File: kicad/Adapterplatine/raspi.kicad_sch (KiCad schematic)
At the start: 8 parts, among them X30 Conn_01x05_Pin, X31 Conn_01x05_Pin, X43 Conn_01x05_Pin

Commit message: Umsortierung/ Erste Leitungung Adapterplatine
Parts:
- added J1: Conn_01x05, Connector_PinSocket_2.54mm:PinSocket_1x05_P2.54mm_Vertical, symbol Connector_Generic:Conn_01x05
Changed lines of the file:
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@@
+	)
+	(symbol
+		(lib_id "Connector_Generic:Conn_01x05")
+		(at 180.34 133.35 270)
+		(unit 1)
+		(body_style 1)
+		(exclude_from_sim no)
+		(in_bom yes)
+		(on_board yes)
+		(in_pos_files yes)
+		(dnp no)
+		(fields_autoplaced yes)
+		(property "Reference" "J1"
+			(at 180.34 137.16 90)
+			(show_name no)
+			(do_not_autoplace no)
+			(effects
+				(font
+					(size 1.27 1.27)
+				)
+			)
+		)
+		(property "Value" "Conn_01x05"
+			(at 180.34 139.7 90)
+			(show_name no)
+			(do_not_autoplace no)
+			(effects
+				(font
+					(size 1.27 1.27)
+				)
+			)
+		)
+		(property "Footprint" "Connector_PinSocket_2.54mm:PinSocket_1x05_P2.54mm_Vertical"
+			(at 180.34 133.35 0)
+			(hide yes)
+			(show_name no)
+			(do_not_autoplace no)
+			(effects
+				(font
+					(size 1.27 1.27)
+				)
+			)
+		)
+		(property "Datasheet" ""
+			(at 180.34 133.35 0)
+			(hide yes)
+			(show_name no)
+			(do_not_autoplace no)
+			(effects
+				(font
+					(size 1.27 1.27)
+				)
+			)
+		)
+		(property "Description" "Generic connector, single row, 01x05, script generated (kicad-library-utils/schlib/autogen/connector/)"
+			(at 180.34 133.35 0)
+			(hide yes)
+			(show_name no)
+			(do_not_autoplace no)
+			(effects
+				(font
+					(size 1.27 1.27)
+				)
+			)
+		)
+		(pin "1"
+		)
+		(pin "3"
+		)
+		(pin "4"
+		)
+		(pin "5"
+		)
+		(pin "2"
+		)
+		(instances
+			(project "Adapterplatine"
+				(path "/99d5d967-6a35-454f-aac3-01cafa1d30b4/6e4113d7-0438-4c79-b883-7b55fbeab670"
+					(reference "J1")
+					(unit 1)
+				)
+			)
+		)
 	)
 	(symbol

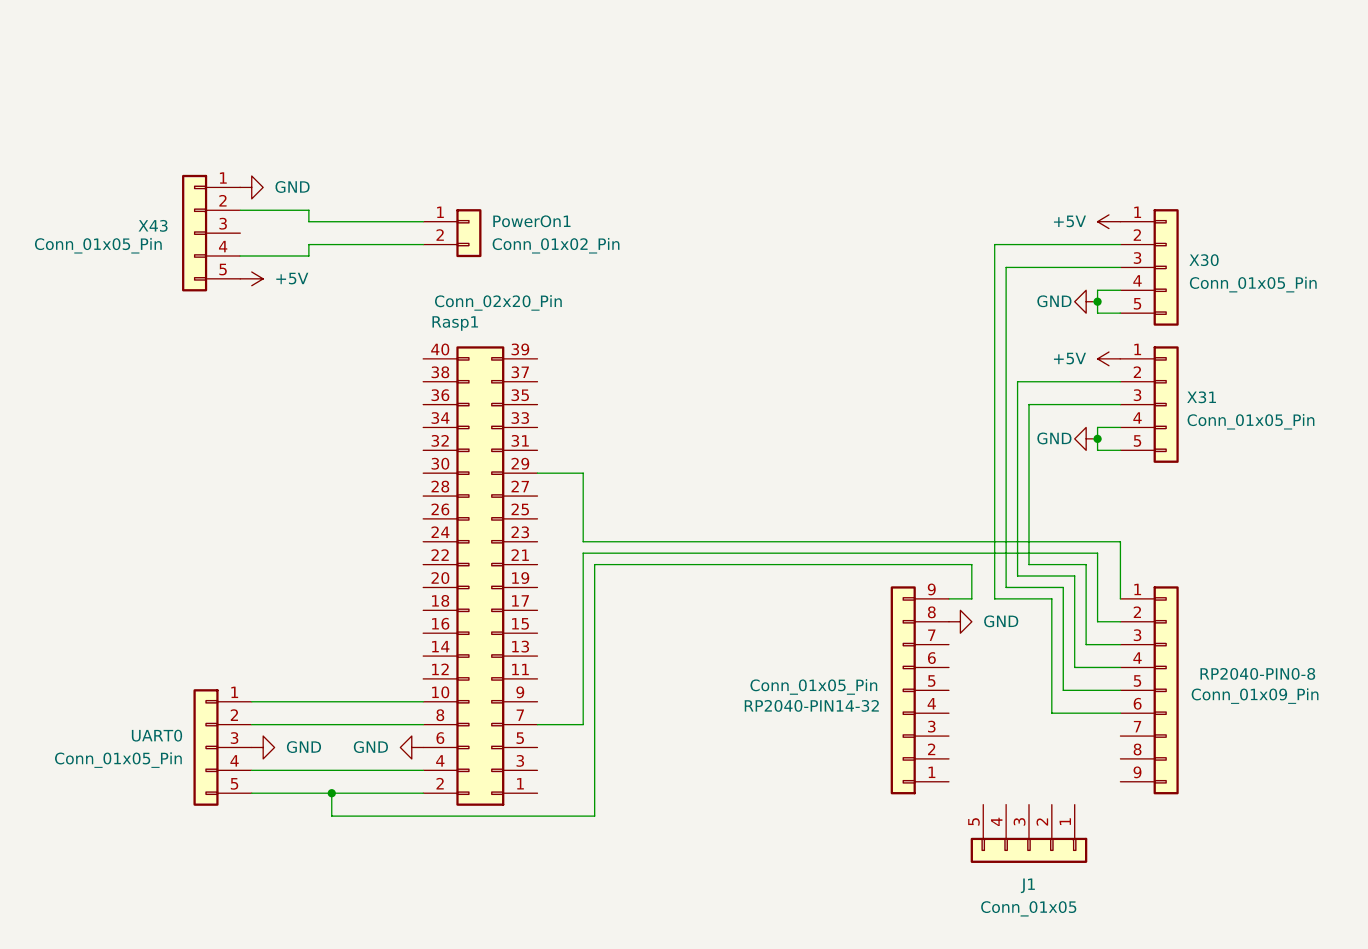
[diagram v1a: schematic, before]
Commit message: Leitungsverlegung Adapterplatine abgeschlossen
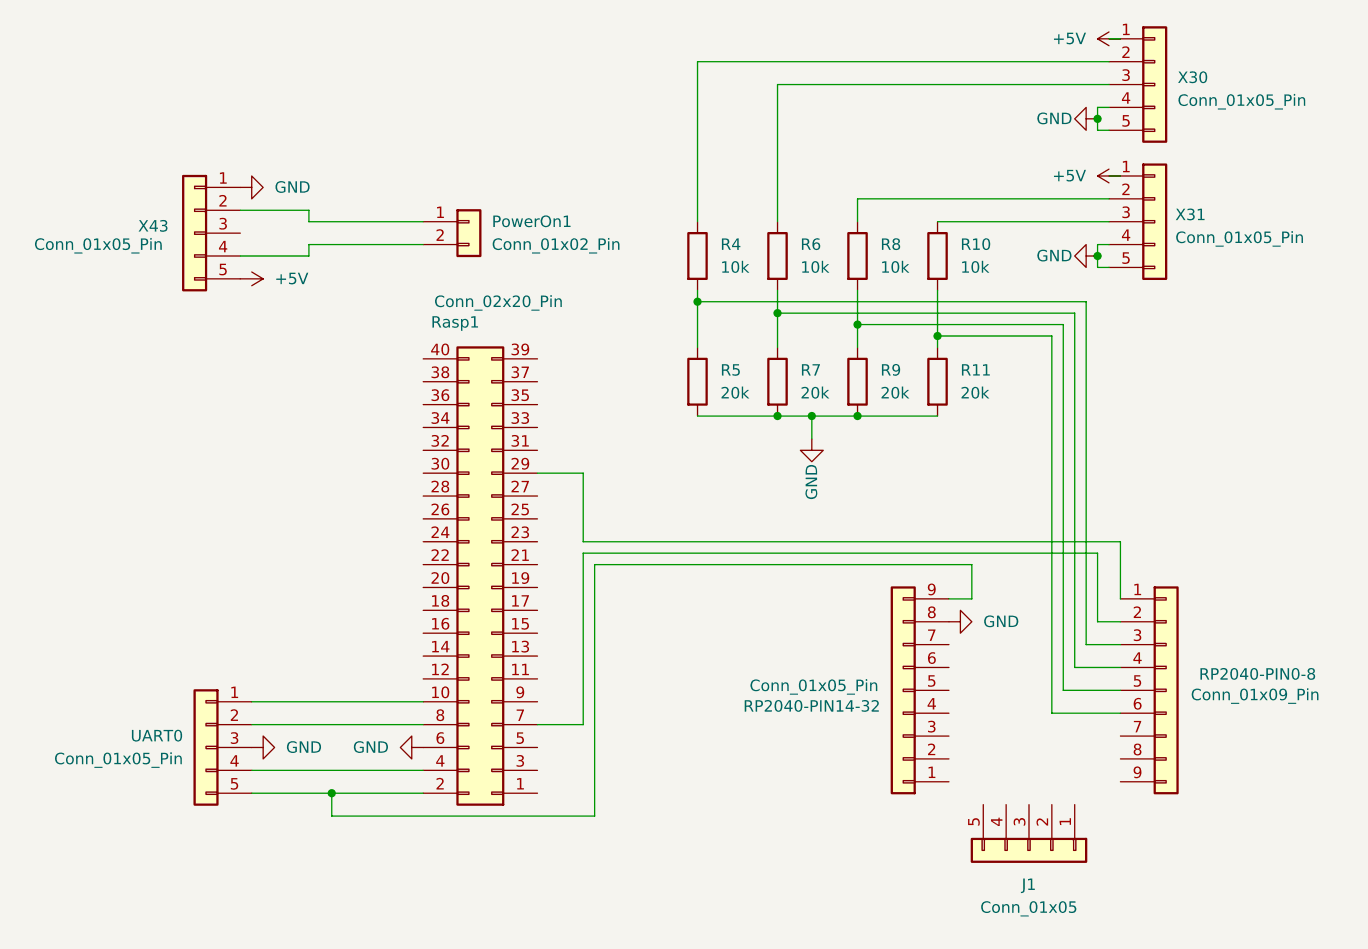
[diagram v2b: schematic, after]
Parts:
- added R10, R4, R6, R8: 10k, Resistor_THT:R_Axial_DIN0207_L6.3mm_D2.5mm_P10.16mm_Horizontal, symbol Device:R
- added R11, R5, R7, R9: 20k, Resistor_THT:R_Axial_DIN0207_L6.3mm_D2.5mm_P10.16mm_Horizontal, symbol Device:R
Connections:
- net GND: now also R11.2, R5.2, R7.2, R9.2
- net at RP2040-PIN0-8.6 (Pin_6): now also R10.2, R11.1; no longer X30.2 (Pin_2)
- net at X30.3 (Pin_3): now also R6.1; no longer RP2040-PIN0-8.5 (Pin_5)
- net at X31.2 (Pin_2): now also R8.1; no longer RP2040-PIN0-8.4 (Pin_4)
- net at X31.3 (Pin_3): now also R10.1; no longer RP2040-PIN0-8.3 (Pin_3)
- new net: R4.1, X30.2 (Pin_2)
- new net: R4.2, R5.1, RP2040-PIN0-8.3 (Pin_3)
- new net: R6.2, R7.1, RP2040-PIN0-8.4 (Pin_4)
- new net: R8.2, R9.1, RP2040-PIN0-8.5 (Pin_5)
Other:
- moved on the sheet: X30, X31

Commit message: Bessere Verlegungen Adapterplatine
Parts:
- RP2040-PIN14-32: value Conn_01x05_Pin -> Conn_01x09_Pin
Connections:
- net at RP2040-PIN14-32.9 (Pin_9), Rasp1.2 (Pin_2): no longer UART0.5 (Pin_5)
- net at Rasp1.4 (Pin_4): no longer UART0.4 (Pin_4)
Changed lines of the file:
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@@
 		(color 0 0 0 0)
 	)
-	(junction
-		(at 102.87 127)
-		(diameter 0)
-		(color 0 0 0 0)
-	)
 	(wire
 		(pts
@@
 	(wire
 		(pts
-			(xy 102.87 127) (xy 102.87 129.54)
+			(xy 107.95 127) (xy 107.95 129.54)
 		)
 		(stroke
@@
 	(wire
 		(pts
+			(xy 107.95 127) (xy 113.03 127)
+		)
+		(stroke
+			(width 0)
+			(type default)
+		)
+	)
+	(wire
+		(pts
 			(xy 186.69 72.39) (xy 186.69 110.49)
 		)
@@
 	(wire
 		(pts
-			(xy 93.98 127) (xy 102.87 127)
-		)
-		(stroke
-			(width 0)
-			(type default)
-		)
-	)
-	(wire
-		(pts
 			(xy 182.88 76.2) (xy 170.18 76.2)
 		)
@@
 	(wire
 		(pts
-			(xy 93.98 124.46) (xy 113.03 124.46)
-		)
-		(stroke
-			(width 0)
-			(type default)
-		)
-	)
-	(wire
-		(pts
 			(xy 152.4 71.12) (xy 152.4 73.66)
 		)
@@
 	(wire
 		(pts
-			(xy 102.87 129.54) (xy 132.08 129.54)
+			(xy 107.95 129.54) (xy 132.08 129.54)
 		)
 		(stroke
@@
 		(pts
 			(xy 161.29 71.12) (xy 161.29 74.93)
-		)
-		(stroke
-			(width 0)
-			(type default)
-		)
-	)
-	(wire
-		(pts
-			(xy 102.87 127) (xy 113.03 127)
 		)
 		(stroke
@@
 			)
 		)
-		(property "Value" "Conn_01x05_Pin"
+		(property "Value" "Conn_01x09_Pin"
 			(at 156.464 115.062 0)
 			(show_name no)

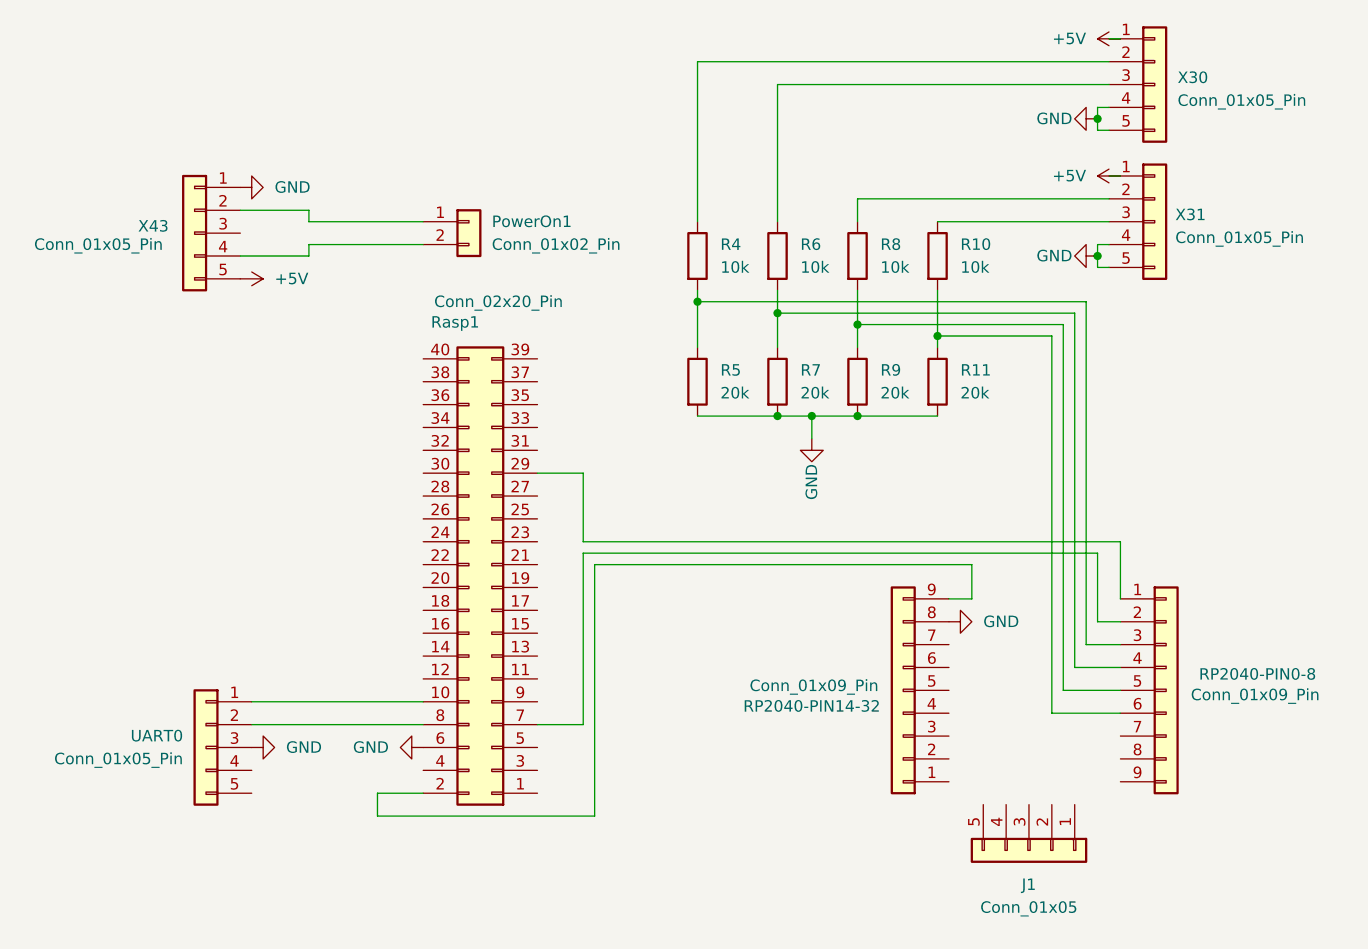
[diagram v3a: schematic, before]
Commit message: Abschlussbericht angefangen/ Adapterplatine ECR DCR
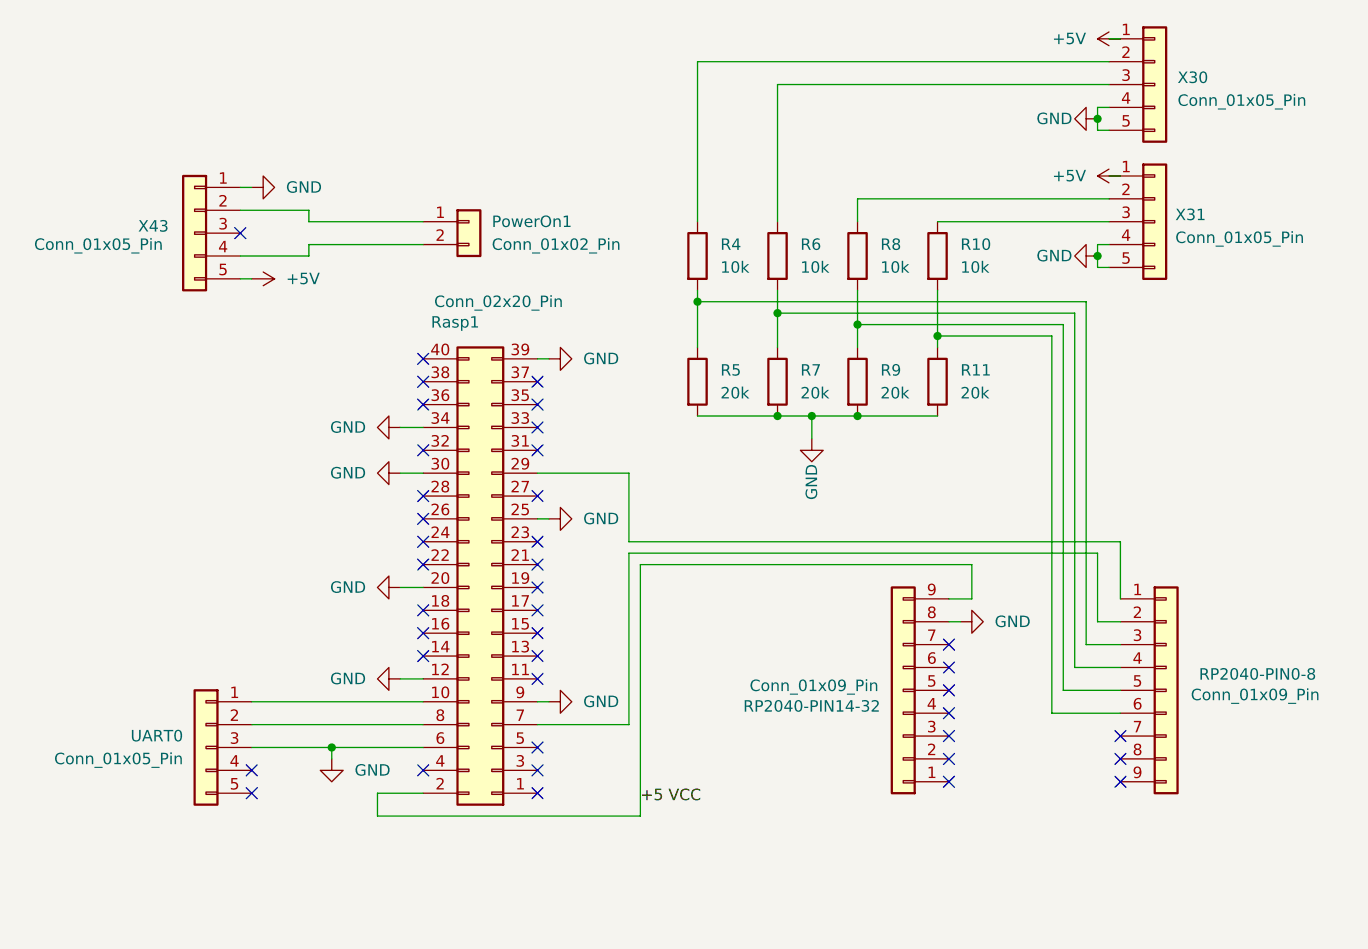
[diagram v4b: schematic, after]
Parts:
- removed J1: Conn_01x05, Connector_PinSocket_2.54mm:PinSocket_1x05_P2.54mm_Vertical, symbol Connector_Generic:Conn_01x05
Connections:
- net GND: now also Rasp1.12 (Pin_12), Rasp1.20 (Pin_20), Rasp1.25 (Pin_25), Rasp1.30 (Pin_30), Rasp1.34 (Pin_34), Rasp1.39 (Pin_39), Rasp1.9 (Pin_9)
- net +5 VCC: now reaches RP2040-PIN14-32.9 (Pin_9), Rasp1.2 (Pin_2)
- no-connect marks 0 -> 40

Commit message: Adapterplatine Gerber
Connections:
- net +5 VCC: now also Rasp1.1 (Pin_1); no longer Rasp1.2 (Pin_2)
- net GND: now also Rasp1.10 (Pin_10), Rasp1.11 (Pin_11), Rasp1.19 (Pin_19), Rasp1.26 (Pin_26), Rasp1.29 (Pin_29), Rasp1.33 (Pin_33), Rasp1.40 (Pin_40), Rasp1.5 (Pin_5); no longer Rasp1.12 (Pin_12), Rasp1.20 (Pin_20), Rasp1.25 (Pin_25), Rasp1.30 (Pin_30), Rasp1.34 (Pin_34), Rasp1.39 (Pin_39), Rasp1.6 (Pin_6), Rasp1.9 (Pin_9)
- net at UART0.1 (Pin_1): now also Rasp1.9 (Pin_9); no longer Rasp1.10 (Pin_10)
- net at RP2040-PIN0-8.1 (Pin_1): now also Rasp1.30 (Pin_30); no longer Rasp1.29 (Pin_29)
- net at Rasp1.7 (Pin_7): now also UART0.2 (Pin_2); no longer RP2040-PIN0-8.2 (Pin_2)
- net at Rasp1.8 (Pin_8): now also RP2040-PIN0-8.2 (Pin_2); no longer UART0.2 (Pin_2)
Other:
- moved on the sheet: Rasp1
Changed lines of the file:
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@@
+	(wire
+		(pts
+			(xy 125.73 91.44) (xy 135.89 91.44)
+		)
+		(stroke
+			(width 0)
+			(type default)
+		)
+	)
 	(wire
 		(pts
@@
 		(pts
 			(xy 93.98 69.85) (xy 92.71 69.85)
-		)
-		(stroke
-			(width 0)
-			(type default)
-		)
-	)
-	(wire
-		(pts
-			(xy 125.73 91.44) (xy 135.89 91.44)
 		)
 		(stroke
@@
 	(symbol
 		(lib_id "Connector_Generic:Conn_02x20_Odd_Even")
-		(at 120.65 104.14 180)
+		(at 118.11 104.14 0)
+		(mirror x)
 		(unit 1)
 		(body_style 1)
@@
 		(dnp no)
 		(property "Reference" "Rasp1"
-			(at 116.586 74.676 0)
+			(at 119.634 74.93 0)
 			(show_name no)
 			(do_not_autoplace no)
@@
 		)
 		(property "Value" "Conn_02x20_Pin"
-			(at 121.412 72.39 0)
+			(at 117.348 72.39 0)
 			(show_name no)
 			(do_not_autoplace no)
@@
 		)
 		(property "Footprint" "Connector_PinHeader_2.54mm:PinHeader_2x20_P2.54mm_Vertical"
-			(at 120.65 104.14 0)
+			(at 118.11 104.14 0)
 			(hide yes)
 			(show_name no)
@@
 		)
 		(property "Datasheet" ""
-			(at 120.65 104.14 0)
+			(at 118.11 104.14 0)
 			(hide yes)
 			(show_name no)
@@
 		)
 		(property "Description" "Generic connector, double row, 02x20, odd/even pin numbering scheme (row 1 odd numbers, row 2 even numbers), script generated (kicad-library-utils/schlib/autogen/connector/)"
-			(at 120.65 104.14 0)
+			(at 118.11 104.14 0)
 			(hide yes)
 			(show_name no)
@@
 		)
 		(property "Hersteller" ""
-			(at 120.65 104.14 0)
+			(at 118.11 104.14 0)
 			(hide yes)
 			(show_name no)
@@
 		)
 		(property "Herstellerbezeichnung" ""
-			(at 120.65 104.14 0)
+			(at 118.11 104.14 0)
 			(hide yes)
 			(show_name no)
@@
 		)
 		(property "Alternative" ""
-			(at 120.65 104.14 0)
-			(hide yes)
-			(show_name no)
+			(at 118.11 104.14 0)
+			(hide yes)
+			(show_name no)
